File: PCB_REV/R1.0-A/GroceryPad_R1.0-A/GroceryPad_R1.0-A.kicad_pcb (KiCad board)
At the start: 2 copper layers, 65 x 36 mm, 5 parts, among them U1 ESP32-C3_SUPERMINI_TH

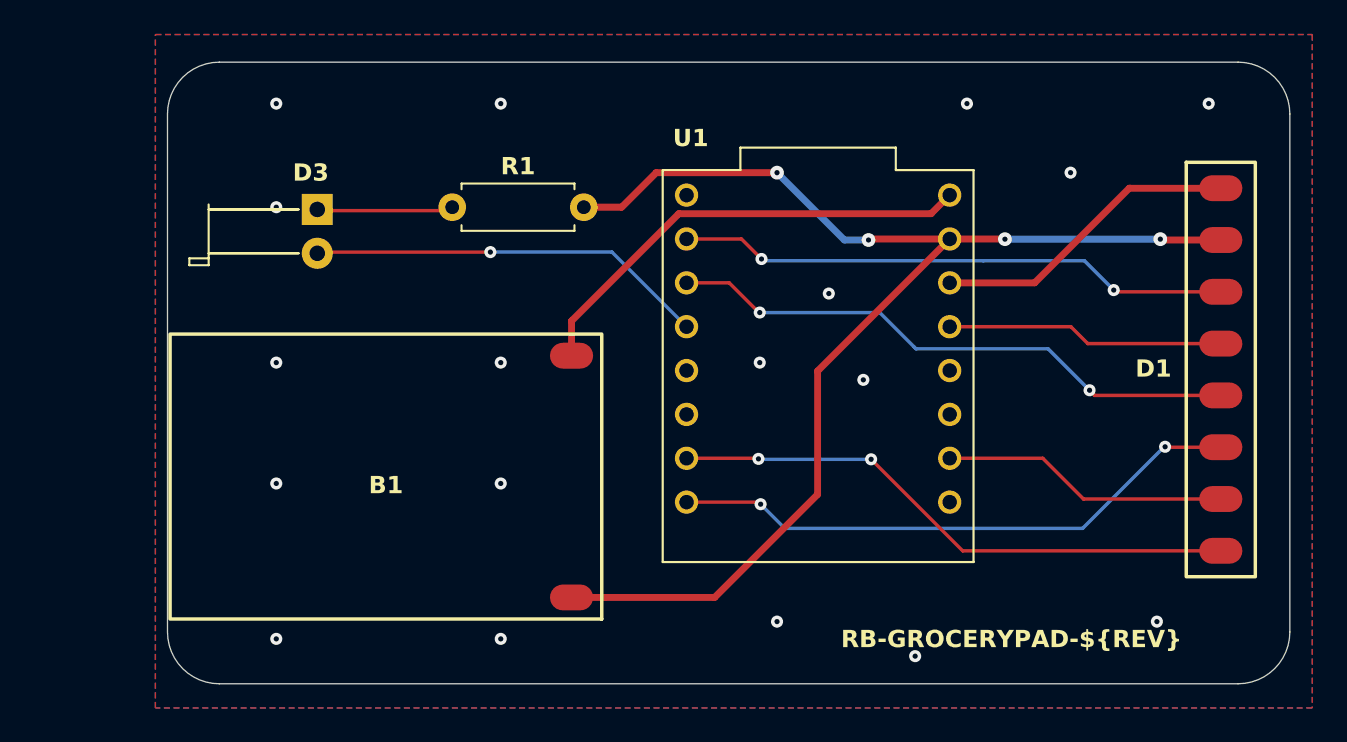
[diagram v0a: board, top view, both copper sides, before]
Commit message: TP4056 breakout footprint
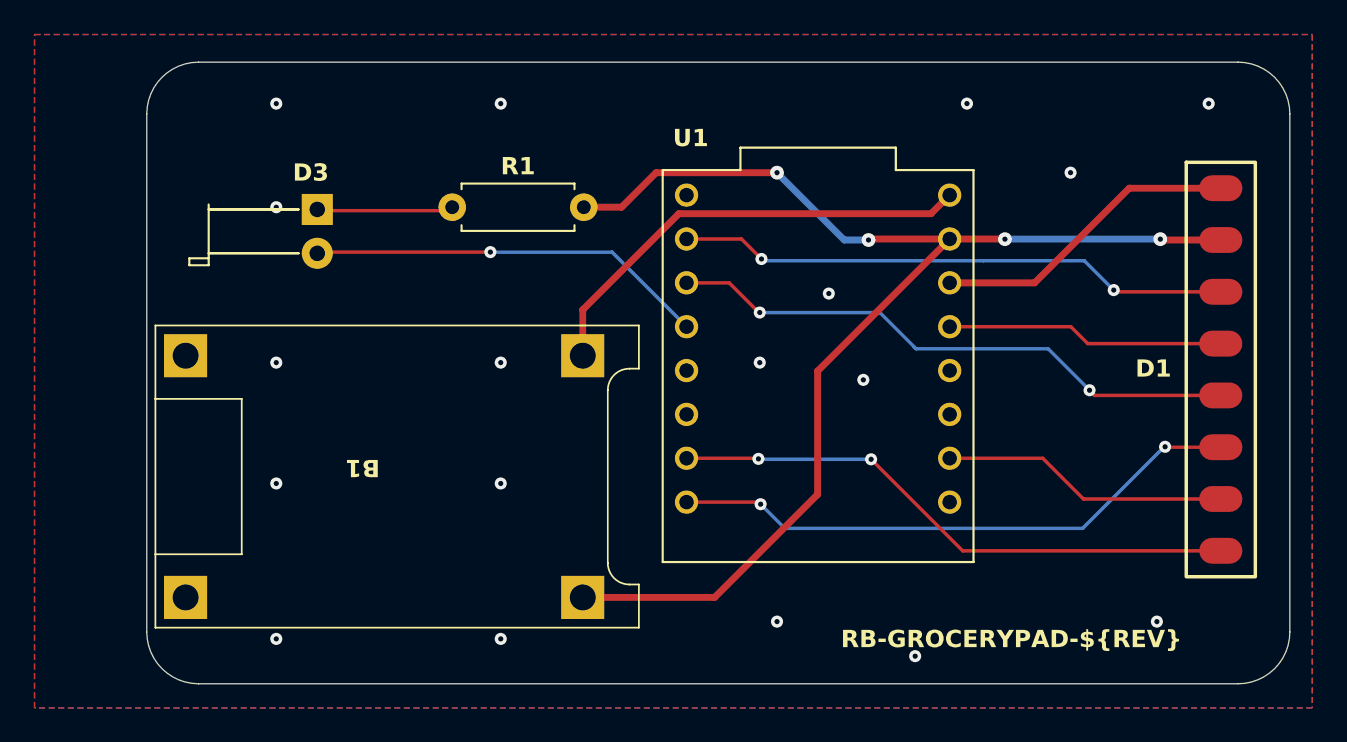
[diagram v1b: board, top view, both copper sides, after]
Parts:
- moved B1 1.35 mm to (200.0, 132.6), turned to 0 degrees
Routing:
- net GND: track 74.2 -> 73.5 mm
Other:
- board size 65 x 36 mm -> 66.2 x 36 mm
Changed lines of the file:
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@@
 		)
 	)
-	(property "DATE" "11/23/25")
+	(property "DATE" "11/26/25")
 	(property "REV" "R1.0-A")
 	(net 0 "")
@@
 	(footprint "TP4056_BOB:HiLetgo TP4056 BOB"
 		(layer "F.Cu")
-		(at 201.35 132.6 180)
+		(at 200 132.6)
 		(descr "Solder pads to connect wires from BOB outputs")
 		(property "Reference" "B1"
-			(at 0 -0.5 0)
+			(at 0 -0.5 180)
 			(unlocked yes)
 			(layer "F.SilkS")
@@
 		)
 		(property "Value" "~"
-			(at 0 1 180)
+			(at 0 1 0)
 			(unlocked yes)
 			(layer "F.Fab")
@@
 		)
 		(property "Datasheet" ""
-			(at 0 0 180)
+			(at 0 0 0)
 			(unlocked yes)
 			(layer "F.Fab")
@@
 		)
 		(property "Description" ""
-			(at 0 0 180)
+			(at 0 0 0)
 			(unlocked yes)
 			(layer "F.Fab")
@@
 		(sheetfile "GroceryPad_R1.0-A.kicad_sch")
 		(attr smd exclude_from_bom)
+		(fp_line
+			(start -12 -8.75)
+			(end 16 -8.75)
+			(stroke
+				(width 0.1)
+				(type default)
+			)
+			(layer "F.SilkS")
+		)
+		(fp_line
+			(start -12 -4.5)
+			(end -12 -8.75)
+			(stroke
+				(width 0.1)
+				(type solid)
+			)
+			(layer "F.SilkS")
+		)
+		(fp_line
+			(start -12 -4.5)
+			(end -12 4.5)
+			(stroke
+				(width 0.1)
+				(type default)
+			)
+			(layer "F.SilkS")
+		)
+		(fp_line
+			(start -12 -4.5)
+			(end -7 -4.5)
+			(stroke
+				(width 0.1)
+				(type default)
+			)
+			(layer "F.SilkS")
+		)
+		(fp_line
+			(start -12 8.75)
+			(end -12 4.5)
+			(stroke
+				(width 0.1)
+				(type solid)
+			)
+			(layer "F.SilkS")
+		)
+		(fp_line
+			(start -7 -4.5)
+			(end -7 4.5)
+			(stroke
+				(width 0.1)
+				(type default)
+			)
+			(layer "F.SilkS")
+		)
+		(fp_line
+			(start -7 4.5)
+			(end -12 4.5)
+			(stroke
+				(width 0.1)
+				(type default)
+			)
+			(layer "F.SilkS")
+		)
+		(fp_line
+			(start 14.2 -5)
+			(end 14.2 5)
+			(stroke
+				(width 0.1)
+				(type solid)
+			)
+			(layer "F.SilkS")
+		)
+		(fp_line
+			(start 16 -8.75)
+			(end 16 -6.25)
+			(stroke
+				(width 0.1)
+				(type solid)
+			)
+			(layer "F.SilkS")
+		)
+		(fp_line
+			(start 16 -6.25)
+			(end 15.45 -6.25)
+			(stroke
+				(width 0.1)
+				(type default)
+			)
+			(layer "F.SilkS")
+		)
+		(fp_line
+			(start 16 6.25)
+			(end 15.45 6.25)
+			(stroke
+				(width 0.1)
+				(type default)
+			)
+			(layer "F.SilkS")
+		)
+		(fp_line
+			(start 16 6.25)
+			(end 16 8.75)
+			(stroke
+				(width 0.1)
+				(type solid)
+			)
+			(layer "F.SilkS")
+		)
+		(fp_line
+			(start 16 8.75)
+			(end -12 8.75)
+			(stroke
+				(width 0.1)
+				(type solid)
+			)
+			(layer "F.SilkS")
+		)
+		(fp_arc
+			(start 14.2 -5)
+			(mid 14.566117 -5.883883)
+			(end 15.45 -6.25)
+			(stroke
+				(width 0.1)
+				(type default)
+			)
+			(layer "F.SilkS")
+		)
+		(fp_arc
+			(start 15.45 6.25)
+			(mid 14.566117 5.883883)
+			(end 14.2 5)
+			(stroke
+				(width 0.1)
+				(type default)
+			)
+			(layer "F.SilkS")
+		)
 		(fp_rect
-			(start -12.5 -8.25)
-			(end 12.5 8.25)
-			(stroke
-				(width 0.2)
-				(type solid)
+			(start -12.25 -9)
+			(end 16.25 9)
+			(stroke
+				(width 0.05)
+				(type default)
 			)
 			(fill no)
-			(layer "F.SilkS")
+			(layer "F.CrtYd")
 		)
 		(fp_text user "${REFERENCE}"
-			(at 0 2.5 180)
-			(unlocked yes)
-			(layer "F.Fab")
-			(effects
-				(font
-					(size 1 1)
-					(thickness 0.15)
-				)
-			)
-		)
-		(pad "3" smd oval
-			(at -10.75 7 180)
-			(size 2.5 1.5)
-			(layers "F.Cu" "F.Mask" "F.Paste")
+			(at 0 2.5 0)
+			(unlocked yes)
+			(layer "F.Fab")
+			(effects
+				(font
+					(size 1 1)
+					(thickness 0.15)
+				)
+			)
+		)
+		(pad "" np_thru_hole rect
+			(at -10.25 -7 180)
+			(size 2.5 2.5)
+			(drill 1.5)
+			(layers "*.Cu" "*.Mask")
+			(pinfunction "OUT+")
+			(pintype "power_out")
+		)
+		(pad "" np_thru_hole rect
+			(at -10.25 7 180)
+			(size 2.5 2.5)
+			(drill 1.5)
+			(layers "*.Cu" "*.Mask")
+			(pinfunction "OUT+")
+			(pintype "power_out")
+		)
+		(pad "3" thru_hole rect
+			(at 12.75 -7 180)
+			(size 2.5 2.5)
+			(drill 1.5)
+			(layers "*.Cu" "*.Mask")
+			(remove_unused_layers no)
 			(net 2 "5V")
 			(pinfunction "OUT+")
 			(pintype "power_out")
 		)
-		(pad "4" smd oval
-			(at -10.75 -7 180)
-			(size 2.5 1.5)
-			(layers "F.Cu" "F.Mask" "F.Paste")
+		(pad "4" thru_hole rect
+			(at 12.75 7 180)
+			(size 2.5 2.5)
+			(drill 1.5)
+			(layers "*.Cu" "*.Mask")
+			(remove_unused_layers no)
 			(net 1 "GND")
 			(pinfunction "OUT-")
@@
 	)
 	(gr_arc
-		(start 188.7 111.6)
-		(mid 189.57868 109.47868)
-		(end 191.7 108.6)
+		(start 187.5 111.6)
+		(mid 188.37868 109.47868)
+		(end 190.5 108.6)
 		(stroke
 			(width 0.05)
@@
 	)
 	(gr_line
-		(start 191.7 144.6)
+		(start 190.5 144.6)
 		(end 250.7 144.6)
 		(stroke
@@
 	(gr_line
 		(start 250.7 108.6)
-		(end 191.7 108.6)
+		(end 190.5 108.6)
 		(stroke
 			(width 0.05)
@@
 	)
 	(gr_line
-		(start 188.7 111.6)
-		(end 188.7 141.6)
+		(start 187.5 111.6)
+		(end 187.5 141.6)
 		(stroke
 			(width 0.05)
@@
 	)
 	(gr_arc
-		(start 191.7 144.6)
-		(mid 189.57868 143.72132)
-		(end 188.7 141.6)
+		(start 190.5 144.6)
+		(mid 188.37868 143.72132)
+		(end 187.5 141.6)
 		(stroke
 			(width 0.05)
@@
 		(layer "F.Fab")
 		(pts
-			(xy 188.7 111.6) (xy 253.7 111.6)
-		)
-		(height -6)
+			(xy 187.5 111.6) (xy 253.7 111.6)
+		)
+		(height -6.9)
 		(orientation 0)
 		(format
@@
 			(keep_text_aligned yes)
 		)
-		(gr_text "65"
-			(at 221.2 103.8 0)
+		(gr_text "66.2"
+			(at 220.6 102.9 0)
 			(layer "F.Fab")
 			(effects
@@
 			)
 		)
+	)
+	(segment
+		(start 226.35 126.49)
+		(end 234 118.84)
+		(width 0.4)
+		(layer "F.Cu")
+		(net 1)
 	)
 	(segment
@@
 	)
 	(segment
+		(start 220.387925 139.6)
+		(end 226.35 133.637925)
+		(width 0.4)
+		(layer "F.Cu")
+		(net 1)
+	)
+	(segment
 		(start 212.81 117)
 		(end 215 117)
@@
 	)
 	(segment
-		(start 220.387925 139.6)
-		(end 226.35 133.637925)
+		(start 249.7 118.9)
+		(end 246.25 118.9)
+		(width 0.4)
+		(layer "F.Cu")
+		(net 1)
+	)
+	(segment
+		(start 212.75 139.6)
+		(end 220.387925 139.6)
+		(width 0.4)
+		(layer "F.Cu")
+		(net 1)
+	)
+	(segment
+		(start 229.3 118.9)
+		(end 229.36 118.84)
 		(width 0.4)
 		(layer "F.Cu")
@@
 	)
 	(segment
-		(start 249.7 118.9)
-		(end 246.25 118.9)
-		(width 0.4)
-		(layer "F.Cu")
-		(net 1)
-	)
-	(segment
-		(start 229.3 118.9)
-		(end 229.36 118.84)
-		(width 0.4)
-		(layer "F.Cu")
-		(net 1)
-	)
-	(segment
-		(start 212.1 139.6)
-		(end 214 139.6)
-		(width 0.4)
-		(layer "F.Cu")
-		(net 1)
-	)
-	(segment
 		(start 246.25 118.9)
 		(end 246.2 118.85)
-		(width 0.4)
-		(layer "F.Cu")
-		(net 1)
-	)
-	(segment
-		(start 226.35 126.49)
-		(end 234 118.84)
-		(width 0.4)
-		(layer "F.Cu")
-		(net 1)
-	)
-	(segment
-		(start 214 139.6)
-		(end 220.387925 139.6)
 		(width 0.4)
 		(layer "F.Cu")
@@
 	)
 	(segment
-		(start 218.31472 117.375)
-		(end 232.925 117.375)
+		(start 212.75 125.6)
+		(end 212.75 122.93972)
+		(width 0.4)
+		(layer "F.Cu")
+		(net 2)
+	)
+	(segment
+		(start 212.75 122.93972)
+		(end 218.31472 117.375)
 		(width 0.4)
 		(layer "F.Cu")
@@
 	)
 	(segment
-		(start 212.1 123.58972)
-		(end 218.31472 117.375)
-		(width 0.4)
-		(layer "F.Cu")
-		(net 2)
-	)
-	(segment
-		(start 212.1 125.6)
-		(end 212.1 123.58972)
+		(start 218.31472 117.375)
+		(end 232.925 117.375)
 		(width 0.4)
 		(layer "F.Cu")
@@
 		(polygon
 			(pts
-				(xy 188 107) (xy 255 107) (xy 255 146) (xy 188 146)
-			)
-		)
+				(xy 181 107) (xy 255 107) (xy 255 146) (xy 181 146)
+			)
+		)
